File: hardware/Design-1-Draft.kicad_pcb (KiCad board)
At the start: 2 copper layers, 120 x 100 mm, 32 parts, among them J1 Barrel_Jack_Switch, M1 WATERPUMP-1, M2 WATERPUMP-2, Q1 IRLZ44N, Q2 IRLZ44N, SW1 Button, U3 ADS1115IDGS, U5 Tang_Nano_9K

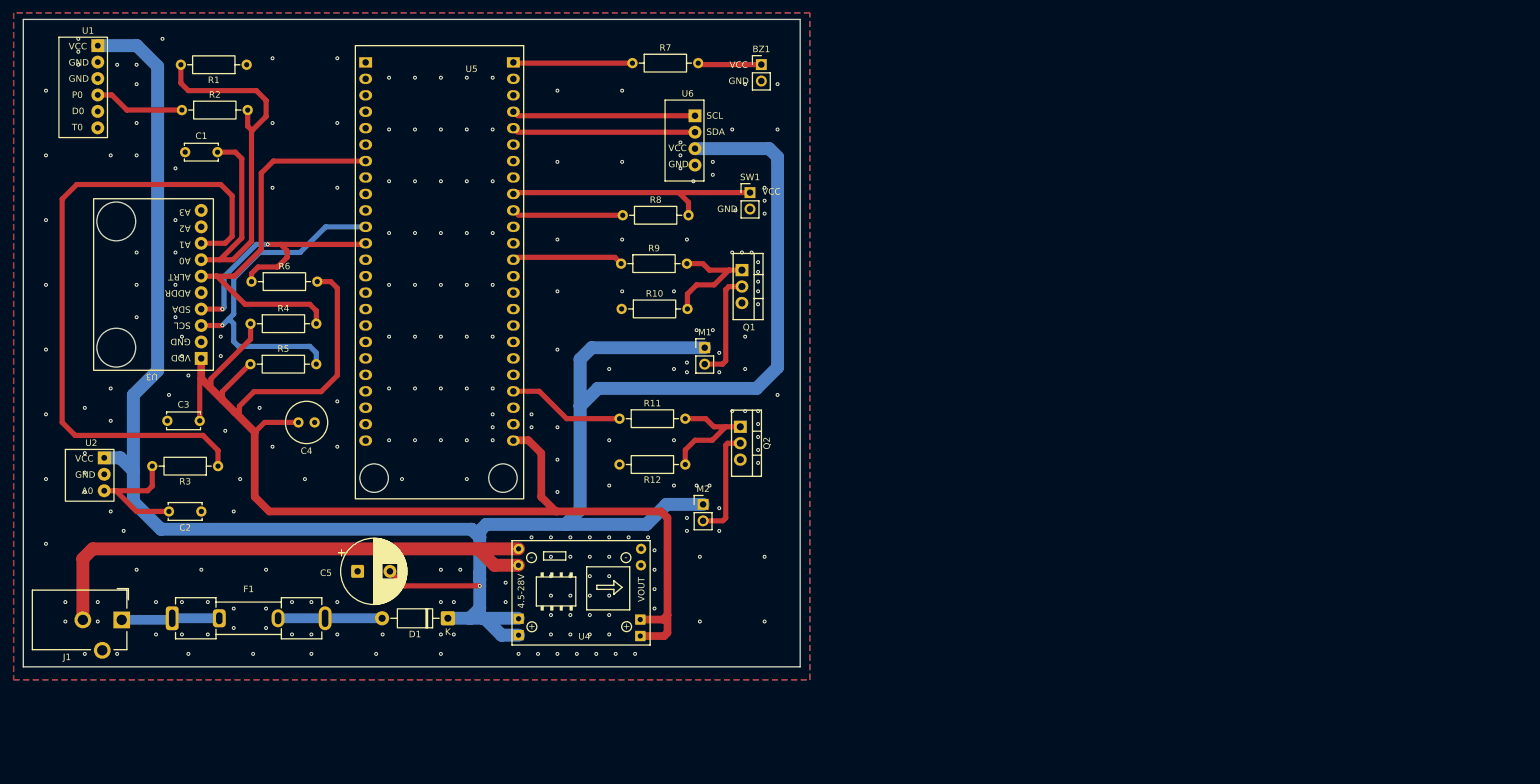
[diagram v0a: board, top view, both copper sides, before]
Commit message: schem: buck converter added > one ground plane pcb: NEW component placement, need traces and ground fills
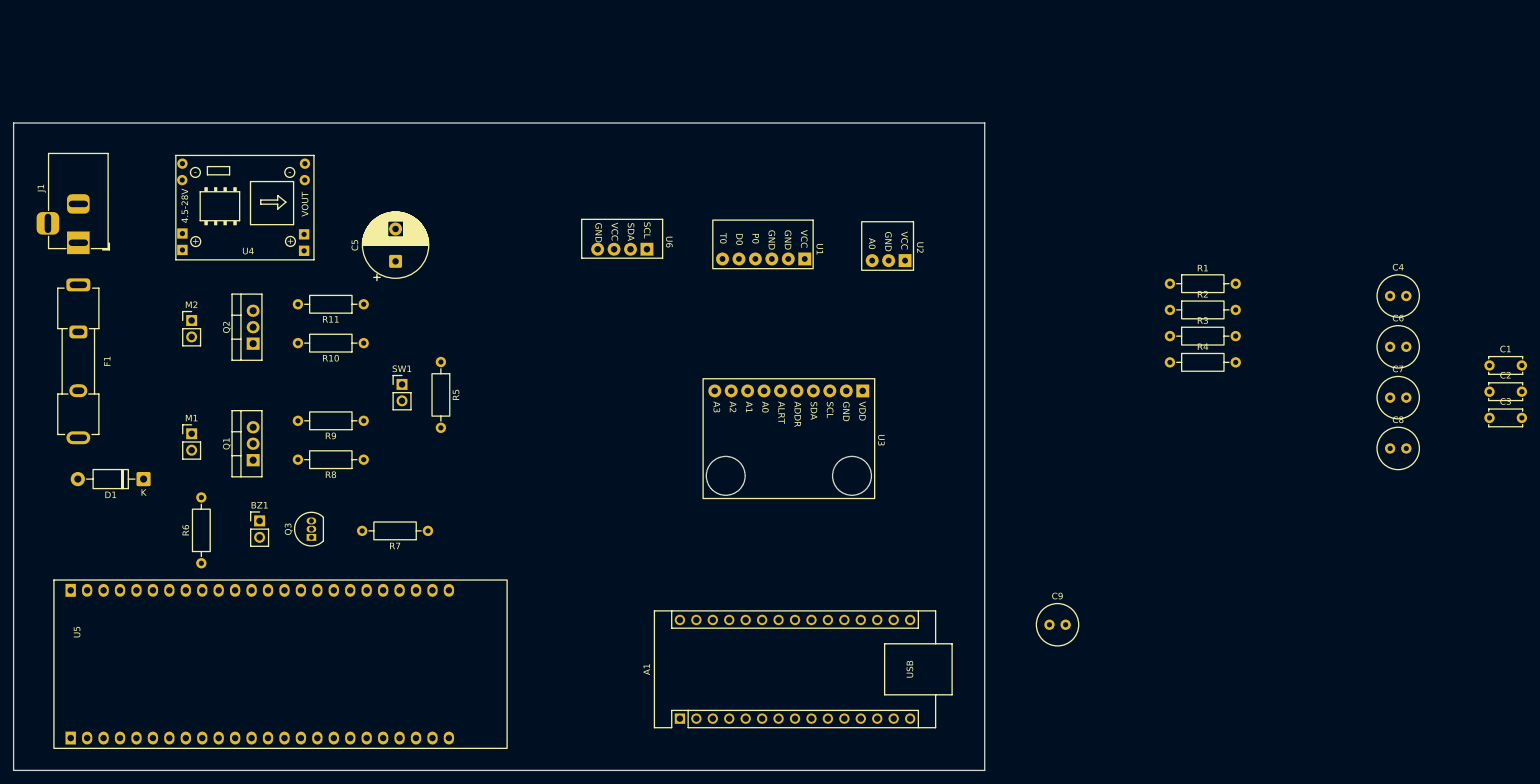
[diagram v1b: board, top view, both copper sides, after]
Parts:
- removed R12: 10k, Resistor_THT:R_Axial_DIN0207_L6.3mm_D2.5mm_P10.16mm_Horizontal
- added A1: Arduino_Nano_ESP32, Module:Arduino_Nano, F.Cu at (167.9, 142.0)
- added C6: 10u, Capacitor_THT:C_Radial_D6.3mm_H5.0mm_P2.50mm, F.Cu at (277.6, 84.6)
- added C7: 10u, Capacitor_THT:C_Radial_D6.3mm_H5.0mm_P2.50mm, F.Cu at (277.6, 92.4)
- added C8: 100u, Capacitor_THT:C_Radial_D6.3mm_H5.0mm_P2.50mm, F.Cu at (277.6, 100.3)
- added C9: 100n, Capacitor_THT:C_Radial_D6.3mm_H5.0mm_P2.50mm, F.Cu at (225.0, 127.5)
- added Q3: PN2222A, Package_TO_SOT_THT:TO-92_Inline, F.Cu at (111.0, 114.0)
- C5: value 470u -> 1000u
- J1: footprint Connector_BarrelJack:BarrelJack_CUI_PJ-102AH_Horizontal -> Connector_BarrelJack:BarrelJack_Horizontal
- R1: value 22k -> 1k
- R10, R8: value 10k -> 100
- R11, R9: value 100 -> 10k
- R2: value 12k -> 1k
- R3: value 1k -> 4.7k
- R5, R6: value 4.7k -> 10k
- R7: value 100 -> 1k
- U3: value ADS1115IDGS -> ADS1115
- moved C3 204.2 mm to (293.0, 95.5)
- moved C1 204.1 mm to (293.0, 87.5)
- moved C2 199.8 mm to (293.0, 91.5), turned to 0 degrees
- moved C4 167.3 mm to (277.6, 76.7), turned to 0 degrees
- moved R2 155.7 mm to (243.6, 78.9)
- moved R3 148.4 mm to (243.6, 82.9), turned to 0 degrees
- moved R1 146.6 mm to (243.6, 74.8), turned to 0 degrees
- moved R4 142.1 mm to (243.6, 87.0)
- moved U2 128.2 mm to (200.0, 69.0), turned to -90 degrees
- moved U1 107.9 mm to (181.0, 69.0), turned to -90 degrees
- moved BZ1 104.8 mm to (103.0, 111.5)
- moved U3 102.2 mm to (186.0, 99.0), turned to -90 degrees
- moved M2 84.0 mm to (92.5, 80.5)
- moved Q1 81.0 mm to (102.0, 102.1), turned to 90 degrees
- moved M1 80.4 mm to (92.5, 98.0)
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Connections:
- BZ1 pad 1: Net-(BZ1-+) -> Net-(A1-VIN)
- BZ1 pad 2: GND -> Net-(BZ1--)
- C1 pad 1: GND -> Net-(A1-VIN)
- C1 pad 2: Net-(U3-AIN0) -> GND
- C3 pad 1: GND -> Net-(A1-VIN)
- C3 pad 2: Net-(U3-VDD) -> GND
- C4 pad 1: GND -> Net-(A1-VIN)
- C4 pad 2: Net-(U3-VDD) -> GND
- C5 pad 2: Net-(D1-K) -> Net-(A1-VIN)
- M1 pad 1: Net-(D1-K) -> Net-(A1-VIN)
- M2 pad 1: Net-(D1-K) -> Net-(A1-VIN)
- R1 pad 1: GND -> Net-(U1-P0)
- R10 pad 1: GND -> Net-(U5-31_IOB15A)
- R10 pad 2: Net-(Q1-G) -> Net-(Q2-G)
- R11 pad 1: Net-(U5-31_IOB15A) -> Net-(Q2-G)
- R11 pad 2: Net-(Q2-G) -> GND
- R2 pad 1: Net-(U1-P0) -> Net-(U3-AIN1)
- R2 pad 2: Net-(U3-AIN0) -> Net-(U2-A0)
- R3 pad 1: Net-(U3-AIN1) -> Net-(A1-VIN)
- R3 pad 2: Net-(U2-A0) -> Net-(A1-SDA/A4)
- R4 pad 1: Net-(U3-VDD) -> Net-(A1-SCL/A5)
- R4 pad 2: Net-(U3-ALERT/RDY) -> Net-(A1-VIN)
- R5 pad 1: Net-(U3-VDD) -> Net-(U5-3V3)
- R5 pad 2: Net-(U3-SCL) -> Net-(U5-69_IOT42A)
- R6 pad 1: Net-(U3-SDA) -> GND
- R6 pad 2: Net-(U3-VDD) -> Net-(A1-VIN)
- R7 pad 1: Net-(U5-63_IOR5A) -> Net-(U5-77_IOT37A)
- R7 pad 2: Net-(BZ1-+) -> Net-(Q3-B)
- R8 pad 1: Net-(U5-77_IOT37A) -> Net-(U5-74_IOT38B)
- R8 pad 2: Net-(U5-79_IOT12B_1V8) -> Net-(Q1-G)
- R9 pad 1: Net-(U5-74_IOT38B) -> GND
- SW1 pad 1: Net-(U5-79_IOT12B_1V8) -> GND
- SW1 pad 2: GND -> Net-(U5-69_IOT42A)
- U1 pad 6: Net-(D1-K) -> Net-(A1-VIN)
- U2 pad 1: Net-(D1-K) -> Net-(A1-VIN)
- U3 pad 10: Net-(U3-SCL) -> Net-(A1-SDA/A4)
- U3 pad 2: Net-(U3-ALERT/RDY) -> unconnected-(U3-ALERT/RDY-Pad2)
- U3 pad 8: Net-(U3-VDD) -> Net-(A1-VIN)
- U3 pad 9: Net-(U3-SDA) -> Net-(A1-SCL/A5)
- U4 pad 3: Net-(U3-VDD) -> Net-(A1-VIN)
- U5 pad 11: Net-(U3-SCL) -> unconnected-(U5-33_IOB23A-Pad11)
- U5 pad 12: Net-(U3-SDA) -> unconnected-(U5-34_IOB23B-Pad12)
- U5 pad 14: unconnected-(U5-35_IOB29A-Pad14) -> Net-(U5-35_IOB29A)
- U5 pad 24: unconnected-(U5-69_IOT42A-Pad24) -> Net-(U5-69_IOT42A)
- U5 pad 25: Net-(U3-VDD) -> Net-(U5-3V3)
- U5 pad 31: unconnected-(U5-5V-Pad31) -> Net-(A1-VIN)
- U5 pad 40: Net-(U5-79_IOT12B_1V8) -> unconnected-(U5-79_IOT12B_1V8-Pad40)
- U5 pad 44: Net-(U5-83_IOT10B_1V8) -> unconnected-(U5-83_IOT10B_1V8-Pad44)
- U5 pad 45: Net-(U5-84_IOT10A_1V8) -> unconnected-(U5-84_IOT10A_1V8-Pad45)
- U5 pad 48: Net-(U5-63_IOR5A) -> unconnected-(U5-63_IOR5A-Pad48)
- U5 pad 7: Net-(U3-ALERT/RDY) -> unconnected-(U5-27_IOB11A-Pad7)
- U6 pad 1: Net-(U5-84_IOT10A_1V8) -> Net-(A1-SDA/A4)
- U6 pad 2: Net-(U5-83_IOT10B_1V8) -> Net-(A1-SCL/A5)
- U6 pad 3: Net-(D1-K) -> Net-(A1-VIN)
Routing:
- net Net-(D1-K): track 348.4 -> 0.00 mm, vias 1 -> 0
- net Net-(U3-VDD): track 202.1 -> 0.00 mm
- net Net-(U3-AIN1): track 102.2 -> 0.00 mm
- net Net-(U4-IN-): track 84.8 -> 0.00 mm
- net Net-(U3-AIN0): track 73.4 -> 0.00 mm
- net Net-(U3-ALERT/RDY): track 59.4 -> 0.00 mm
- net Net-(U3-SCL): track 54.0 -> 0.00 mm, vias 1 -> 0
- net Net-(U3-SDA): track 42.6 -> 0.00 mm, vias 2 -> 0
- net Net-(U5-79_IOT12B_1V8): track 41.4 -> 0.00 mm
- net Net-(U5-84_IOT10A_1V8): track 28.3 -> 0.00 mm
- net Net-(U5-83_IOT10B_1V8): track 28.3 -> 0.00 mm
- net Net-(U2-A0): track 20.3 -> 0.00 mm
- net Net-(Q2-G): track 19.5 -> 0.00 mm
- net Net-(Q1-G): track 19.2 -> 0.00 mm
- net Net-(U5-63_IOR5A): track 18.4 -> 0.00 mm
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- removed copper zone on B.Cu, net GND
- removed copper zone on F.Cu, net GND
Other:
- board size 120 x 100 mm -> 150 x 100 mm
- board text removed: "GND"
- board text removed: "VCC"

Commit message: updated pcb, traces & ground fills pa
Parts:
- added REF**: CONV_BOB-12009, 1_CustomFootprints:CONV_BOB-12009, F.Cu at (153.9, 137.8)
- moved A1 13.0 mm to (167.1, 129.0)
- moved U3 10.3 mm to (181.0, 90.0)

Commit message: updated PCB, traces and ground fills pa
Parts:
- moved C1 117.9 mm to (175.5, 77.9)
- moved C2 117.9 mm to (175.5, 82.0)
- moved C3 117.9 mm to (175.5, 86.0)
- moved R1 86.7 mm to (156.9, 76.8)
- moved R2 86.7 mm to (156.9, 80.9)
- moved R3 86.7 mm to (156.9, 85.0)
- moved R4 86.7 mm to (156.9, 89.0)
- moved C4 74.8 mm to (203.0, 81.3)
- moved C6 74.8 mm to (203.0, 89.2)
- moved C7 74.8 mm to (203.0, 97.0)
- moved C8 74.8 mm to (203.0, 104.8)
- moved C9 25.7 mm to (202.0, 116.0)
- moved U3 15.0 mm to (181.0, 105.0)
- moved A1 14.5 mm to (170.8, 143.0)
- moved REF** 3.81 mm to (154.0, 134.0)
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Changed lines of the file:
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@@
 	(footprint "Capacitor_THT:C_Radial_D6.3mm_H5.0mm_P2.50mm"
 		(layer "F.Cu")
-		(at 277.62 84.57)
+		(at 203 89.15)
 		(descr "C, Radial series, Radial, pin pitch=2.50mm, diameter=6.3mm, height=5mm, Non-Polar Electrolytic Capacitor")
 		(tags "C Radial series Radial pin pitch 2.50mm diameter 6.3mm height 5mm Non-Polar Electrolytic Capacitor")
@@
 	(footprint "Resistor_THT:R_Axial_DIN0207_L6.3mm_D2.5mm_P10.16mm_Horizontal"
 		(layer "F.Cu")
-		(at 243.61 86.97)
+		(at 156.92 89)
 		(descr "Resistor, Axial_DIN0207 series, Axial, Horizontal, pin pitch=10.16mm, 0.25W = 1/4W, length*diameter=6.3*2.5mm^2, http://cdn-reichelt.de/documents/datenblatt/B400/1_4W%23YAG.pdf")
 		(tags "Resistor Axial_DIN0207 series Axial Horizontal pin pitch 10.16mm 0.25W = 1/4W length 6.3mm diameter 2.5mm")
@@
 	(footprint "Resistor_THT:R_Axial_DIN0207_L6.3mm_D2.5mm_P10.16mm_Horizontal"
 		(layer "F.Cu")
-		(at 243.61 82.92)
+		(at 156.92 84.95)
 		(descr "Resistor, Axial_DIN0207 series, Axial, Horizontal, pin pitch=10.16mm, 0.25W = 1/4W, length*diameter=6.3*2.5mm^2, http://cdn-reichelt.de/documents/datenblatt/B400/1_4W%23YAG.pdf")
 		(tags "Resistor Axial_DIN0207 series Axial Horizontal pin pitch 10.16mm 0.25W = 1/4W length 6.3mm diameter 2.5mm")
@@
 	(footprint "Capacitor_THT:C_Radial_D6.3mm_H5.0mm_P2.50mm"
 		(layer "F.Cu")
-		(at 277.62 76.72)
+		(at 203 81.3)
 		(descr "C, Radial series, Radial, pin pitch=2.50mm, diameter=6.3mm, height=5mm, Non-Polar Electrolytic Capacitor")
 		(tags "C Radial series Radial pin pitch 2.50mm diameter 6.3mm height 5mm Non-Polar Electrolytic Capacitor")
@@
 	(footprint "Capacitor_THT:C_Radial_D6.3mm_H5.0mm_P2.50mm"
 		(layer "F.Cu")
-		(at 225 127.5)
+		(at 202 116)
 		(descr "C, Radial series, Radial, pin pitch=2.50mm, diameter=6.3mm, height=5mm, Non-Polar Electrolytic Capacitor")
 		(tags "C Radial series Radial pin pitch 2.50mm diameter 6.3mm height 5mm Non-Polar Electrolytic Capacitor")
@@
 	(footprint "Diode_THT:D_DO-41_SOD81_P10.16mm_Horizontal"
 		(layer "F.Cu")
-		(at 85.08 105 180)
+		(at 85.08 106 180)
 		(descr "Diode, DO-41_SOD81 series, Axial, Horizontal, pin pitch=10.16mm, length*diameter=5.2*2.7mm^2, https://www.diodes.com/assets/Package-Files/DO-41-Plastic.pdf")
 		(tags "Diode DO-41_SOD81 series Axial Horizontal pin pitch 10.16mm  length 5.2mm diameter 2.7mm")
@@
 	(footprint "Resistor_THT:R_Axial_DIN0207_L6.3mm_D2.5mm_P10.16mm_Horizontal"
 		(layer "F.Cu")
-		(at 243.61 78.87)
+		(at 156.92 80.9)
 		(descr "Resistor, Axial_DIN0207 series, Axial, Horizontal, pin pitch=10.16mm, 0.25W = 1/4W, length*diameter=6.3*2.5mm^2, http://cdn-reichelt.de/documents/datenblatt/B400/1_4W%23YAG.pdf")
 		(tags "Resistor Axial_DIN0207 series Axial Horizontal pin pitch 10.16mm 0.25W = 1/4W length 6.3mm diameter 2.5mm")
@@
 	(footprint "1_CustomFootprints:CONV_BOB-12009"
 		(layer "F.Cu")
-		(at 153.92 137.81)
+		(at 154 134)
 		(property "Reference" "REF**"
 			(at -3.325 -9.135 0)
@@
 	(footprint "1_CustomFootprints:ADS1115"
 		(layer "F.Cu")
-		(at 181 90 -90)
+		(at 181 105 -90)
 		(property "Reference" "U3"
 			(at 0 -13 270)
@@
 	(footprint "Capacitor_THT:C_Radial_D6.3mm_H5.0mm_P2.50mm"
 		(layer "F.Cu")
-		(at 277.62 100.27)
+		(at 203 104.85)
 		(descr "C, Radial series, Radial, pin pitch=2.50mm, diameter=6.3mm, height=5mm, Non-Polar Electrolytic Capacitor")
 		(tags "C Radial series Radial pin pitch 2.50mm diameter 6.3mm height 5mm Non-Polar Electrolytic Capacitor")
@@
 	(footprint "Capacitor_THT:C_Disc_D5.0mm_W2.5mm_P5.00mm"
 		(layer "F.Cu")
-		(at 292.97 87.45)
+		(at 175.5 77.9)
 		(descr "C, Disc series, Radial, pin pitch=5.00mm, diameter*width=5*2.5mm^2, Capacitor, http://cdn-reichelt.de/documents/datenblatt/B300/DS_KERKO_TC.pdf")
 		(tags "C Disc series Radial pin pitch 5.00mm diameter 5mm width 2.5mm Capacitor")
@@
 	(footprint "Capacitor_THT:C_Radial_D6.3mm_H5.0mm_P2.50mm"
 		(layer "F.Cu")
-		(at 277.62 92.42)
+		(at 203 97)
 		(descr "C, Radial series, Radial, pin pitch=2.50mm, diameter=6.3mm, height=5mm, Non-Polar Electrolytic Capacitor")
 		(tags "C Radial series Radial pin pitch 2.50mm diameter 6.3mm height 5mm Non-Polar Electrolytic Capacitor")
@@
 	(footprint "Module:Arduino_Nano"
 		(layer "F.Cu")
-		(at 167.06 129 90)
+		(at 170.84 143 90)
 		(descr "Arduino Nano, http://www.mouser.com/pdfdocs/Gravitech_Arduino_Nano3_0.pdf")
 		(tags "Arduino Nano")
@@
 	(footprint "Capacitor_THT:C_Disc_D5.0mm_W2.5mm_P5.00mm"
 		(layer "F.Cu")
-		(at 292.97 95.55)
+		(at 175.5 86)
 		(descr "C, Disc series, Radial, pin pitch=5.00mm, diameter*width=5*2.5mm^2, Capacitor, http://cdn-reichelt.de/documents/datenblatt/B300/DS_KERKO_TC.pdf")
 		(tags "C Disc series Radial pin pitch 5.00mm diameter 5mm width 2.5mm Capacitor")
@@
 	(footprint "Capacitor_THT:C_Disc_D5.0mm_W2.5mm_P5.00mm"
 		(layer "F.Cu")
-		(at 292.97 91.5)
+		(at 175.5 81.95)
 		(descr "C, Disc series, Radial, pin pitch=5.00mm, diameter*width=5*2.5mm^2, Capacitor, http://cdn-reichelt.de/documents/datenblatt/B300/DS_KERKO_TC.pdf")
 		(tags "C Disc series Radial pin pitch 5.00mm diameter 5mm width 2.5mm Capacitor")
@@
 	(footprint "Resistor_THT:R_Axial_DIN0207_L6.3mm_D2.5mm_P10.16mm_Horizontal"
 		(layer "F.Cu")
-		(at 243.61 74.82)
+		(at 156.92 76.85)
 		(descr "Resistor, Axial_DIN0207 series, Axial, Horizontal, pin pitch=10.16mm, 0.25W = 1/4W, length*diameter=6.3*2.5mm^2, http://cdn-reichelt.de/documents/datenblatt/B400/1_4W%23YAG.pdf")
 		(tags "Resistor Axial_DIN0207 series Axial Horizontal pin pitch 10.16mm 0.25W = 1/4W length 6.3mm diameter 2.5mm")

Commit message: Updated PCB & SCHEM
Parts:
- removed C9: 100n, Capacitor_THT:C_Radial_D6.3mm_H5.0mm_P2.50mm
- moved U1 156.5 mm to (65.0, 174.0), turned to 90 degrees
- moved C7 145.5 mm to (59.0, 118.0)
- moved U2 138.9 mm to (109.0, 174.0), turned to 90 degrees
- moved U6 126.5 mm to (89.2, 173.5), turned to 90 degrees
- moved R5 116.0 mm to (47.1, 167.0), turned to 180 degrees
- moved SW1 107.7 mm to (43.6, 161.0), turned to -90 degrees
- moved R7 105.2 mm to (35.9, 64.0), turned to 0 degrees
- moved C8 104.5 mm to (129.0, 31.0), turned to 180 degrees
- moved R6 96.4 mm to (35.9, 41.0), turned to 0 degrees
- moved Q3 92.4 mm to (39.1, 56.0), turned to 0 degrees
- moved R4 91.2 mm to (84.9, 145.0)
- moved R3 89.4 mm to (84.9, 138.0)
- moved BZ1 88.0 mm to (42.0, 48.0), turned to -90 degrees
- moved REF** 82.5 mm to (76.0, 107.0)
- moved C6 82.5 mm to (126.5, 120.0)
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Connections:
- C7 pad 2: AGND -> GND
- C8 pad 1: unconnected-(C8-Pad1) -> GND
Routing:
- net Net-(A1-VIN): track 0.00 -> 123.1 mm
- net Net-(U4-IN-): track 0.00 -> 71.5 mm
- net Net-(D1-K): track 0.00 -> 16.8 mm
- net Net-(F1-Pad1): track 0.00 -> 6.73 mm
- net Net-(D1-A): track 0.00 -> 6.49 mm
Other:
- board size 150 x 100 mm -> 125 x 180 mm
